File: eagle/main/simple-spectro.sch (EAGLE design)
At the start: 54 parts, among them CON1 BAT, CON2 SPI, CON3 SPI, CON4 VIBR, IC1 32U4, IC2 MCP73831T, IC4 DMP1045U or DMG2302, IC5 LM1117S-3.3, Q6 BSP75, U1 TMP75DGK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

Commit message: pcb v1.4 elecrow
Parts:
- R16, R17, R18, R19, R3: value 10K -> 10k
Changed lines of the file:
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@@
 <part name="U$3" library="microbuilder" deviceset="GND" device=""/>
 <part name="U$5" library="microbuilder" deviceset="GND" device=""/>
-<part name="R3" library="rcl" deviceset="R-EU_" device="R0805" value="10K">
+<part name="R3" library="rcl" deviceset="R-EU_" device="R0805" value="10k">
 <attribute name="ELECROW" value="C17414"/>
 <attribute name="LCSC" value="C17414"/>
@@
 <part name="GND6" library="supply1" deviceset="GND" device=""/>
 <part name="GND10" library="supply1" deviceset="GND" device=""/>
-<part name="R16" library="rcl" deviceset="R-EU_" device="R0805" value="10K">
+<part name="R16" library="rcl" deviceset="R-EU_" device="R0805" value="10k">
 <attribute name="ELECROW" value="C17414"/>
 <attribute name="LCSC" value="C17414"/>
 </part>
-<part name="R17" library="rcl" deviceset="R-EU_" device="R0805" value="10K">
+<part name="R17" library="rcl" deviceset="R-EU_" device="R0805" value="10k">
 <attribute name="ELECROW" value="C17414"/>
 <attribute name="LCSC" value="C17414"/>
@@
 <part name="SUPPLY8" library="supply1" deviceset="VCC" device=""/>
 <part name="SUPPLY9" library="supply1" deviceset="VCC" device=""/>
-<part name="R18" library="rcl" deviceset="R-EU_" device="R0805" value="10K">
+<part name="R18" library="rcl" deviceset="R-EU_" device="R0805" value="10k">
 <attribute name="ELECROW" value="C17414"/>
 <attribute name="LCSC" value="C17414"/>
 </part>
-<part name="R19" library="rcl" deviceset="R-EU_" device="R0805" value="10K">
+<part name="R19" library="rcl" deviceset="R-EU_" device="R0805" value="10k">
 <attribute name="ELECROW" value="C17414"/>
 <attribute name="LCSC" value="C17414"/>

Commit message: update value
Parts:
- C7: LCSC C77502 -> C49678
- R11, R15: ELECROW C118844 -> C17407; LCSC C118844 -> C17407
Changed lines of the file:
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@@
 </part>
 <part name="R15" library="rcl" deviceset="R-EU_" device="R0805" value="100k">
-<attribute name="ELECROW" value="C118844"/>
-<attribute name="LCSC" value="C118844"/>
+<attribute name="ELECROW" value="C17407"/>
+<attribute name="LCSC" value="C17407"/>
 <attribute name="MPN" value="RC1206FR-07100KL"/>
 </part>
@@
 <part name="C7" library="rcl" library_urn="urn:adsk.eagle:library:334" deviceset="C-EU" device="C0805K" package3d_urn="urn:adsk.eagle:package:23681/2" value="100nF">
 <attribute name="ELECROW" value="C49678"/>
-<attribute name="LCSC" value="C77502"/>
+<attribute name="LCSC" value="C49678"/>
 <attribute name="MPN" value="80-C1206C104K5R"/>
 </part>
 <part name="R11" library="rcl" library_urn="urn:adsk.eagle:library:334" deviceset="R-EU_" device="R0805" package3d_urn="urn:adsk.eagle:package:23553/2" value="100k">
-<attribute name="ELECROW" value="C118844"/>
-<attribute name="LCSC" value="C118844"/>
+<attribute name="ELECROW" value="C17407"/>
+<attribute name="LCSC" value="C17407"/>
 <attribute name="MPN" value="RC1206FR-07100KL"/>
 </part>

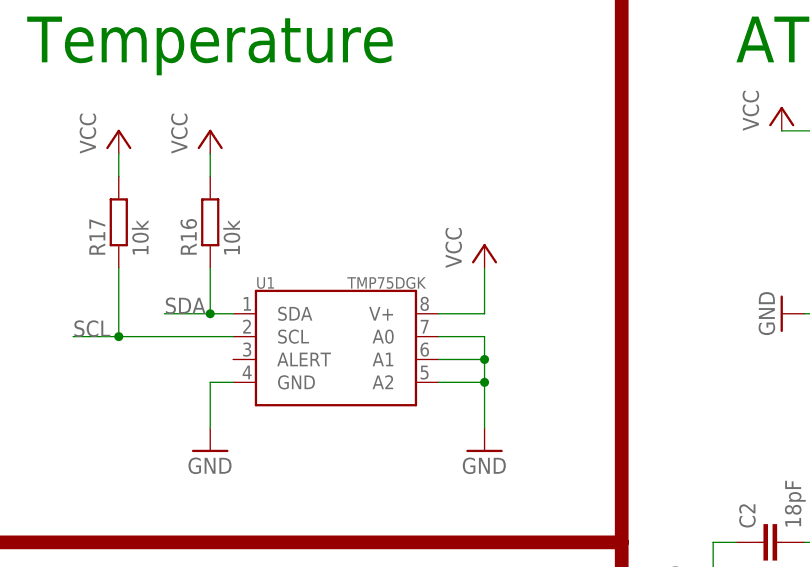
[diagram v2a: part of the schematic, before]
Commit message: add temperature and battery sensor for model B
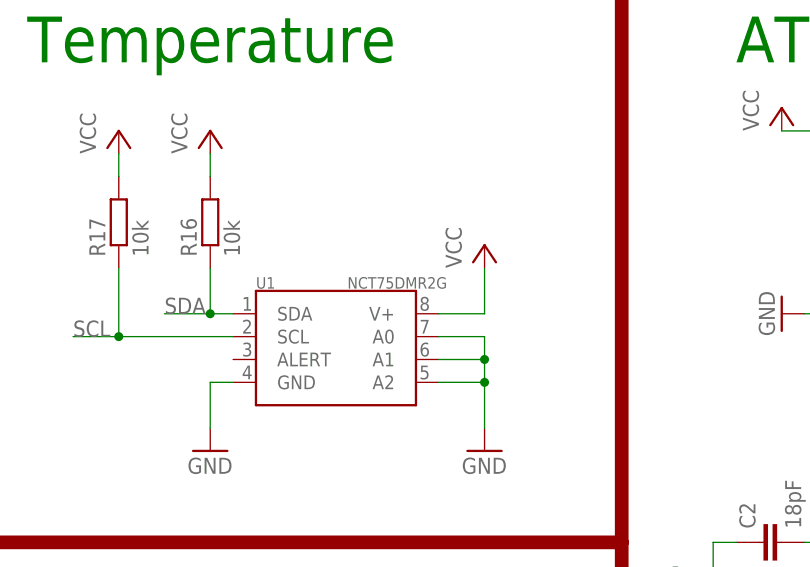
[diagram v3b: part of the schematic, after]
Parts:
- U1: value TMP75DGK -> NCT75DMR2G
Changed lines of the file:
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@@
 <part name="POT" library="dp_devices" deviceset="TRIMMER" device="-3362P" value="10k"/>
 <part name="CON1" library="jumper" deviceset="JP1E" device="" value="BAT"/>
-<part name="U1" library="ti_tmp" deviceset="TMP75" device="DGK">
+<part name="U1" library="ti_tmp" deviceset="TMP75" device="DGK" value="NCT75DMR2G">
 <attribute name="LCSC" value="C94387"/>
 </part>

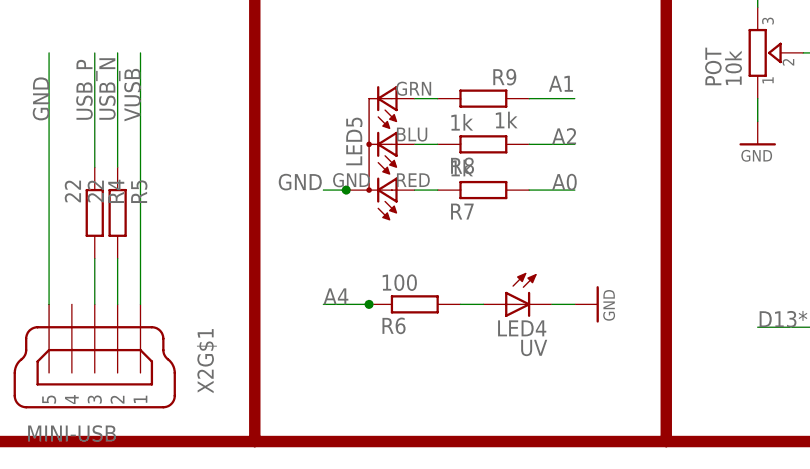
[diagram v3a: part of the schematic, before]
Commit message: add GND labels in eagle
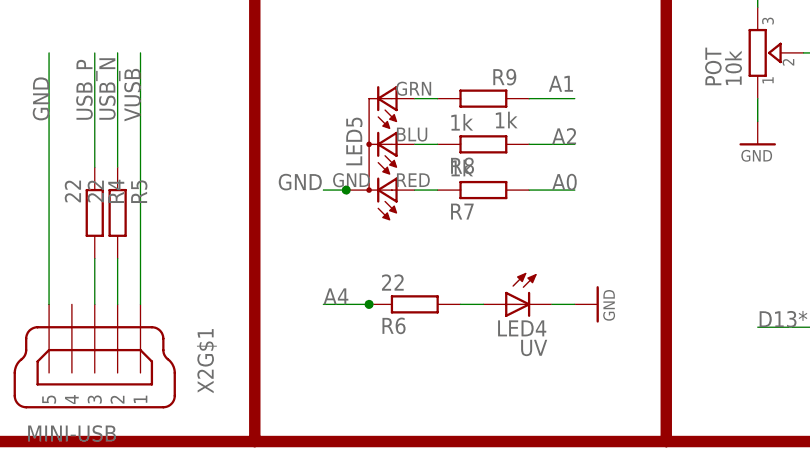
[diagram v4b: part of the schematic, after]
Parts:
- R6: value 100 -> 22; ELECROW C17408 -> C17561; LCSC C17408 -> C17561
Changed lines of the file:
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@@
 <attribute name="MPN" value="621-1N5819HW-F"/>
 </part>
-<part name="R6" library="rcl" deviceset="R-EU_" device="R0805" value="100">
-<attribute name="ELECROW" value="C17408"/>
-<attribute name="LCSC" value="C17408"/>
+<part name="R6" library="rcl" deviceset="R-EU_" device="R0805" value="22">
+<attribute name="ELECROW" value="C17561"/>
+<attribute name="LCSC" value="C17561"/>
 <attribute name="MPN" value="667-ERJ-8GEYJ101V"/>
 </part>

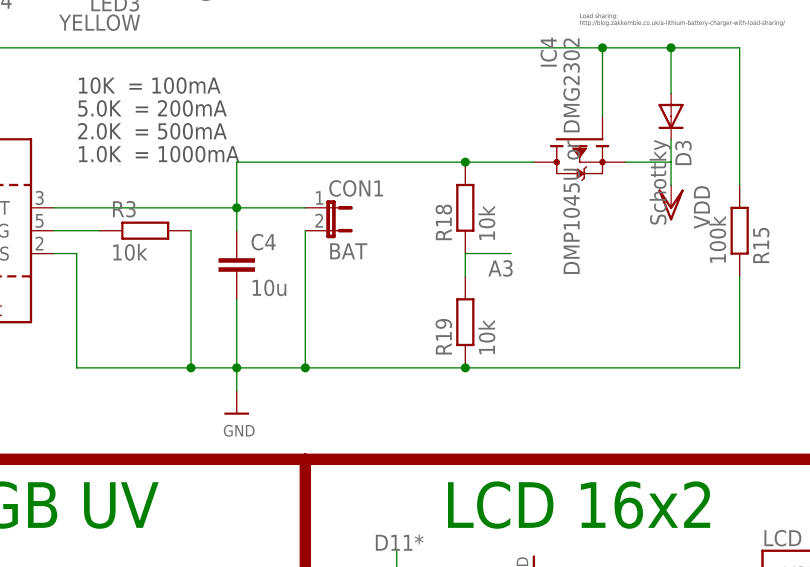
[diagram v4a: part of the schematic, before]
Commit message: change to 1Mohms and add capacitor for battery voltage detection
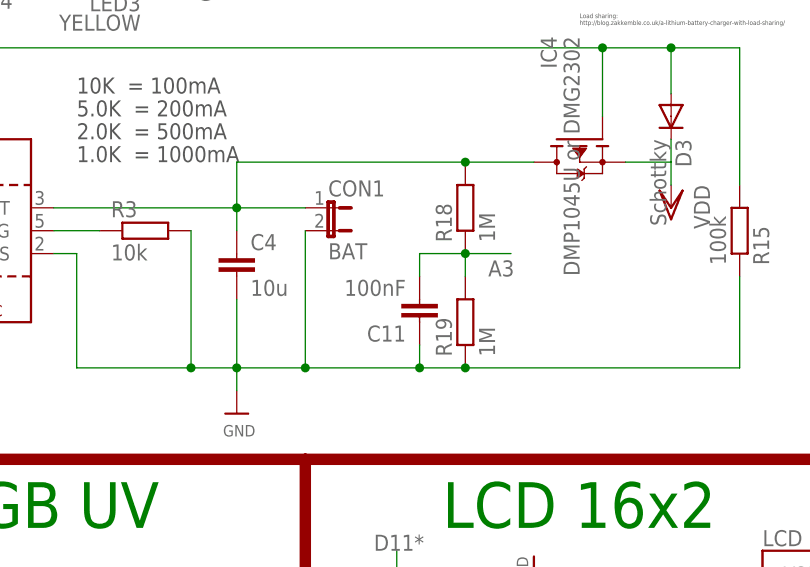
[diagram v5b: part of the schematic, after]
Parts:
- added C11: 100nF, rcl:C-EUC0805K
- R18, R19: value 10k -> 1M; ELECROW C17414 -> C17514; LCSC C17414 -> C17514
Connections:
- net A3: now also C11.2
- net GND: now also C11.1
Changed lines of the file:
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@@
 <part name="SUPPLY8" library="supply1" deviceset="VCC" device=""/>
 <part name="SUPPLY9" library="supply1" deviceset="VCC" device=""/>
-<part name="R18" library="rcl" deviceset="R-EU_" device="R0805" value="10k">
-<attribute name="ELECROW" value="C17414"/>
-<attribute name="LCSC" value="C17414"/>
+<part name="R18" library="rcl" deviceset="R-EU_" device="R0805" value="1M">
+<attribute name="ELECROW" value="C17514"/>
+<attribute name="LCSC" value="C17514"/>
 </part>
-<part name="R19" library="rcl" deviceset="R-EU_" device="R0805" value="10k">
-<attribute name="ELECROW" value="C17414"/>
-<attribute name="LCSC" value="C17414"/>
+<part name="R19" library="rcl" deviceset="R-EU_" device="R0805" value="1M">
+<attribute name="ELECROW" value="C17514"/>
+<attribute name="LCSC" value="C17514"/>
 </part>
 <part name="CON4" library="jumper" deviceset="JP1E" device="" value="VIBR"/>
@@
 <attribute name="LCSC" value="C15850"/>
 <attribute name="MPN" value="77-VJ1206V106ZXQTBC"/>
+</part>
+<part name="C11" library="rcl" library_urn="urn:adsk.eagle:library:334" deviceset="C-EU" device="C0805K" package3d_urn="urn:adsk.eagle:package:23681/2" value="100nF">
+<attribute name="ELECROW" value="C49678"/>
+<attribute name="LCSC" value="C49678"/>
+<attribute name="MPN" value="80-C1206C104K5R"/>
 </part>
 </parts>
@@
 <attribute name="MPN" x="119.38" y="91.44" size="1.778" layer="96" display="off"/>
 </instance>
+<instance part="C11" gate="G$1" x="139.7" y="83.82" rot="R180">
+<attribute name="MPN" x="139.7" y="83.82" size="1.778" layer="96" rot="R180" display="off"/>
+<attribute name="LCSC" x="139.7" y="83.82" size="1.778" layer="96" rot="R180" display="off"/>
+<attribute name="ELECROW" x="139.7" y="83.82" size="1.778" layer="96" rot="R180" display="off"/>
+</instance>
 </instances>
 <busses>
@@
 <wire x1="127" y1="78.74" x2="119.38" y2="78.74" width="0.1524" layer="91"/>
 <junction x="119.38" y="78.74"/>
-<wire x1="127" y1="78.74" x2="144.78" y2="78.74" width="0.1524" layer="91"/>
+<wire x1="127" y1="78.74" x2="139.7" y2="78.74" width="0.1524" layer="91"/>
 <pinref part="R15" gate="G$1" pin="1"/>
+<wire x1="139.7" y1="78.74" x2="144.78" y2="78.74" width="0.1524" layer="91"/>
 <wire x1="144.78" y1="78.74" x2="175.26" y2="78.74" width="0.1524" layer="91"/>
 <wire x1="175.26" y1="88.9" x2="175.26" y2="78.74" width="0.1524" layer="91"/>
@@
 <junction x="144.78" y="78.74"/>
 <pinref part="C4" gate="G$1" pin="2"/>
+<pinref part="C11" gate="G$1" pin="1"/>
+<wire x1="139.7" y1="81.28" x2="139.7" y2="78.74" width="0.1524" layer="91"/>
+<junction x="139.7" y="78.74"/>
 </segment>
 <segment>
@@
 <wire x1="144.78" y1="91.44" x2="149.86" y2="91.44" width="0.1524" layer="91"/>
 <label x="147.32" y="88.9" size="1.778" layer="95"/>
-</segment>
-</net>
+<pinref part="C11" gate="G$1" pin="2"/>
+<wire x1="144.78" y1="91.44" x2="139.7" y2="91.44" width="0.1524" layer="91"/>
+<wire x1="139.7" y1="91.44" x2="139.7" y2="88.9" width="0.1524" layer="91"/>
+<junction x="144.78" y="91.44"/>
+</segment>
+</net>

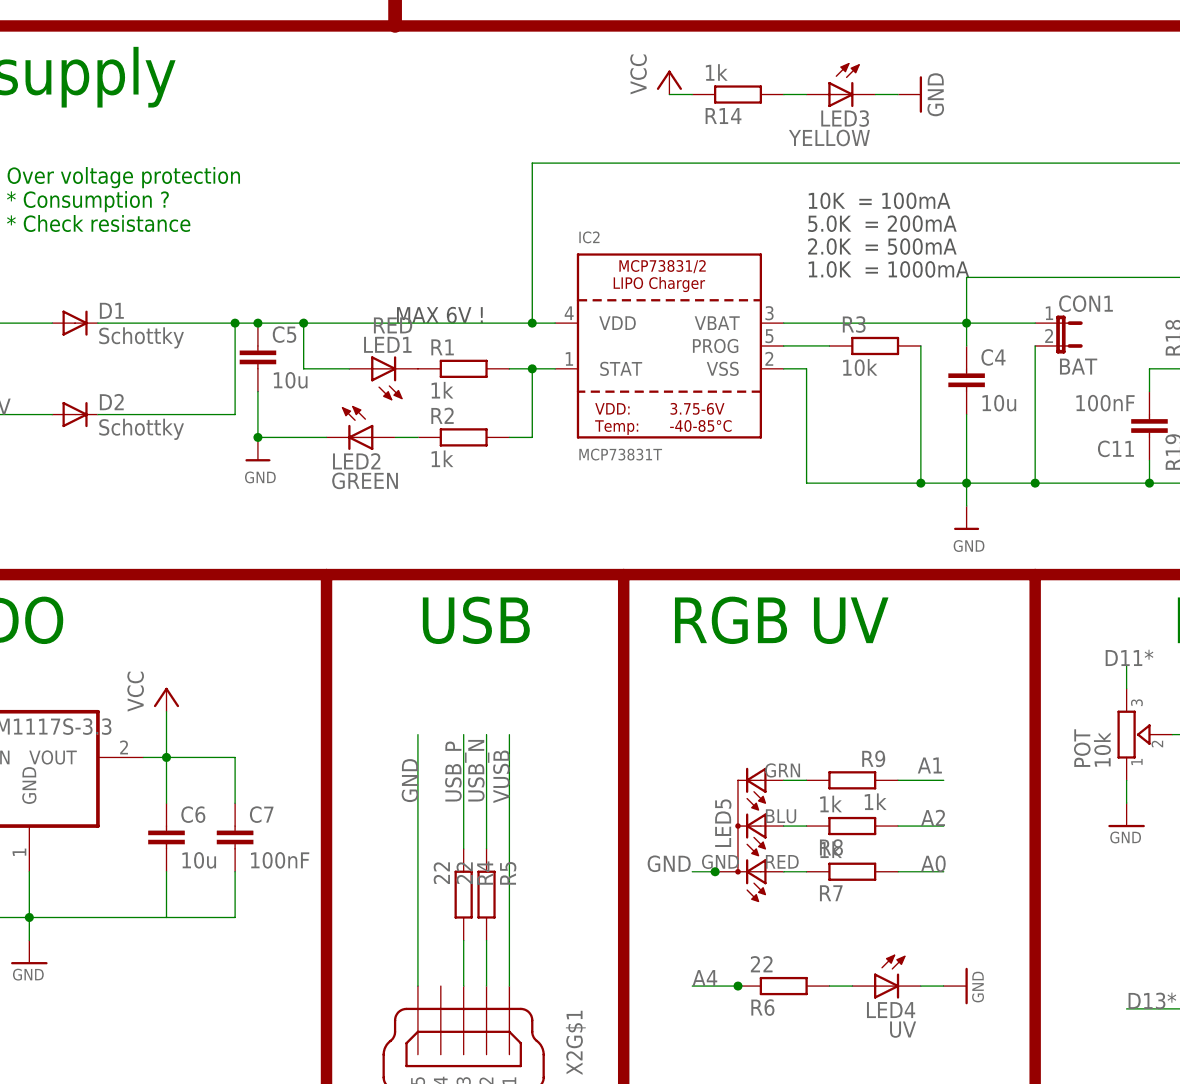
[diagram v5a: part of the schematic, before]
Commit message: pcb 1.4.1 sent for production
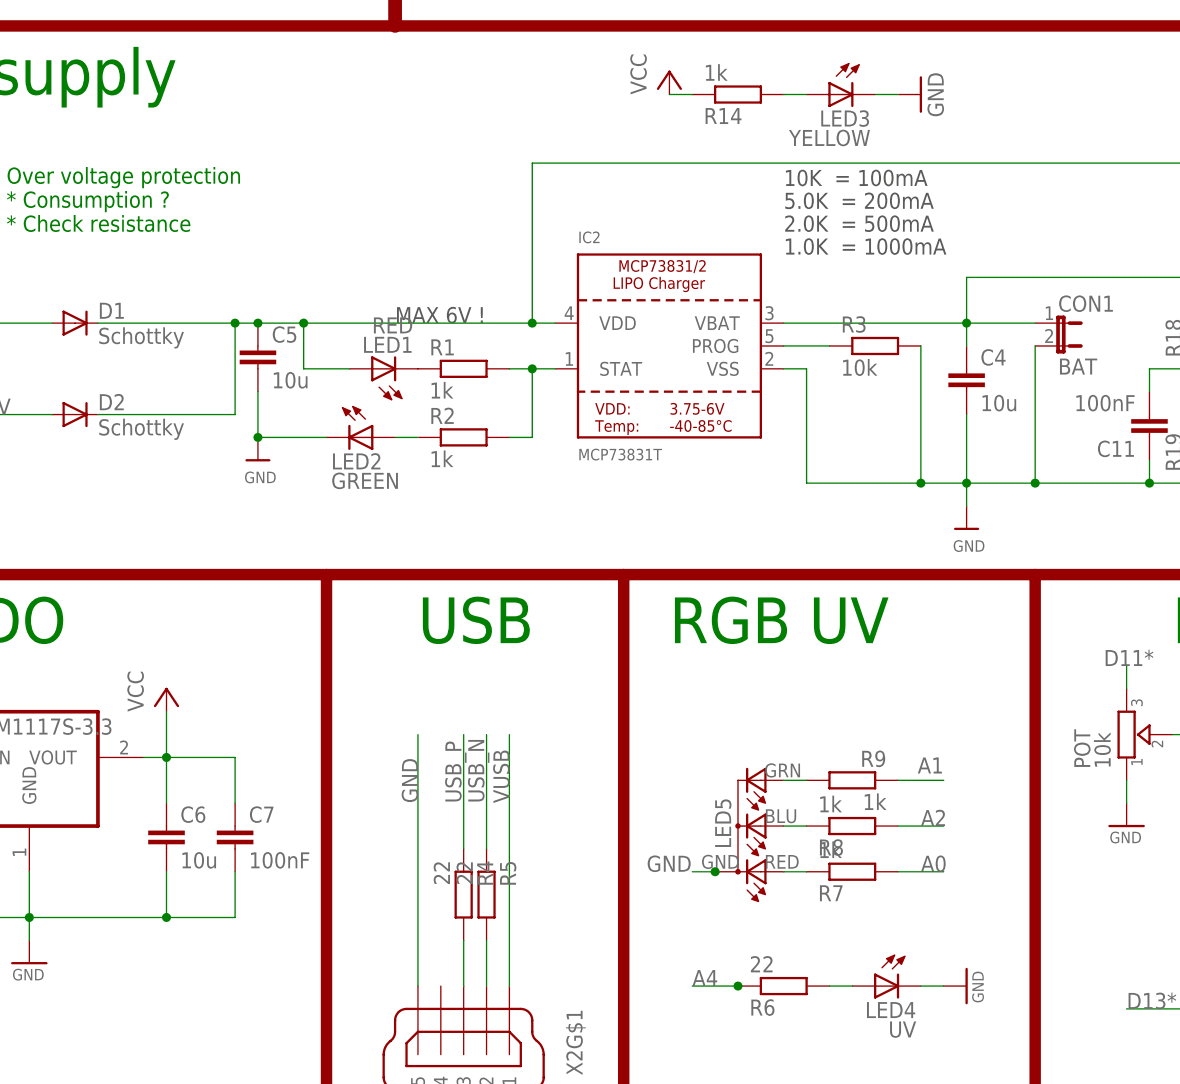
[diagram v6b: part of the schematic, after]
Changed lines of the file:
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@@
 <text x="-10.16" y="60.96" size="5.08" layer="91">3.3V LDO</text>
 <wire x1="127" y1="7.62" x2="127" y2="68.58" width="1.27" layer="94"/>
-<text x="101.6" y="109.22" size="1.778" layer="97">10K  = 100mA</text>
-<text x="101.6" y="106.68" size="1.778" layer="97">5.0K  = 200mA</text>
-<text x="101.6" y="104.14" size="1.778" layer="97">2.0K  = 500mA</text>
-<text x="101.6" y="101.6" size="1.778" layer="97">1.0K  = 1000mA</text>
+<text x="99.06" y="111.76" size="1.778" layer="97">10K  = 100mA</text>
+<text x="99.06" y="109.22" size="1.778" layer="97">5.0K  = 200mA</text>
+<text x="99.06" y="106.68" size="1.778" layer="97">2.0K  = 500mA</text>
+<text x="99.06" y="104.14" size="1.778" layer="97">1.0K  = 1000mA</text>
 <text x="55.88" y="96.52" size="1.778" layer="97">MAX 6V !</text>
 <text x="157.48" y="116.84" size="0.508" layer="97">Load sharing:
@@
 <wire x1="30.48" y1="30.48" x2="38.1" y2="30.48" width="0.1524" layer="91"/>
 <wire x1="38.1" y1="30.48" x2="38.1" y2="35.56" width="0.1524" layer="91"/>
-</segment>
-<segment>
+<junction x="30.48" y="30.48"/>
+</segment>
+<segment>

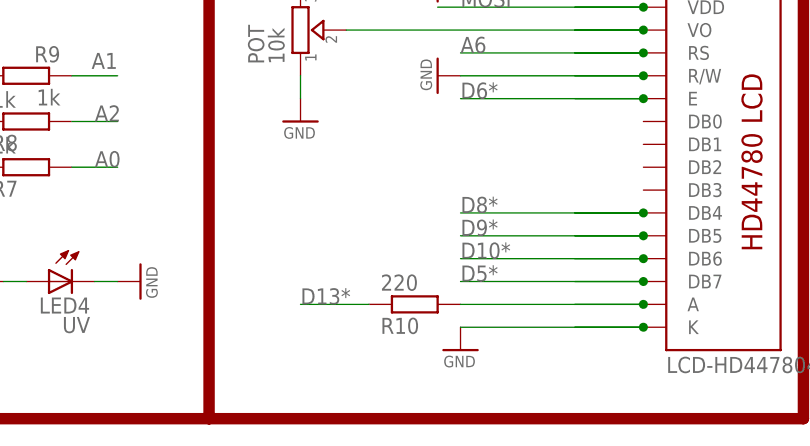
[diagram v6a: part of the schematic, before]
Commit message: fix (PCB): change resistor for backlight to 0 ohm
close #37
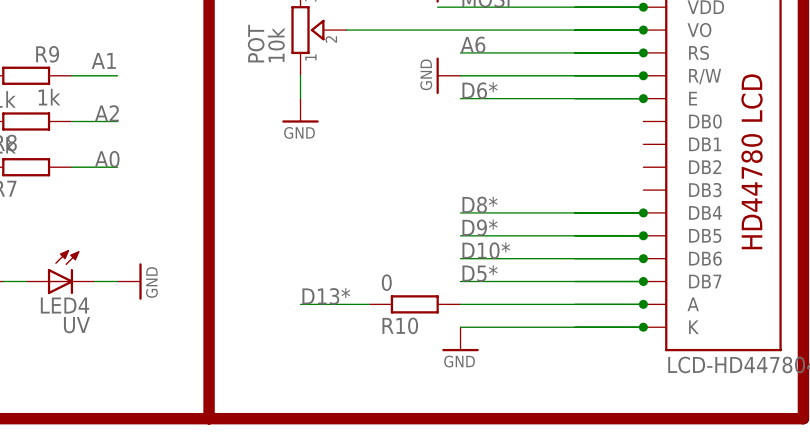
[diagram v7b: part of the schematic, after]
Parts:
- R10: value 220 -> 0; ELECROW C17557 -> C17477; LCSC C17557 -> C17477
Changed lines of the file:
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@@
 <part name="GND3" library="supply1" deviceset="GND" device=""/>
 <part name="GND4" library="supply1" deviceset="GND" device=""/>
-<part name="R10" library="rcl" library_urn="urn:adsk.eagle:library:334" deviceset="R-EU_" device="R0805" package3d_urn="urn:adsk.eagle:package:23553/2" value="220">
-<attribute name="ELECROW" value="C17557"/>
-<attribute name="LCSC" value="C17557"/>
+<part name="R10" library="rcl" library_urn="urn:adsk.eagle:library:334" deviceset="R-EU_" device="R0805" package3d_urn="urn:adsk.eagle:package:23553/2" value="0">
+<attribute name="ELECROW" value="C17477"/>
+<attribute name="LCSC" value="C17477"/>
 </part>
 <part name="U$1" library="lpatiny" deviceset="EC11E" device=""/>
